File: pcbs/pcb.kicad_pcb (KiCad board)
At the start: 2 copper layers, 148.3 x 111.7 mm, 42 parts

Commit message: Convert to Helios (RP2040-based) MCU and add underglow LEDs
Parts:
- removed the ? at (25.7, 7.11) (x4)
- removed J9: , lib:Jumper
- added ?: LOGO, Library:fractalxcu, F.Cu at (153.4, 156.2)
- added ?: LOGO, Library:fractalx, F.Cu at (153.4, 156.2)
- added ?: LOGO, Library:fractalxcu, B.Cu at (153.4, 156.2)
- added ?: LOGO, Library:fractalx, B.Cu at (153.4, 156.2)
- added J1: , lib:Jumper, F.Cu at (219.8, 129.8)
- added LED1, LED7: , WS2812B, F.Cu at (128.8, 99.8)
- added LED10, LED4: , WS2812B, F.Cu at (149.0, 132.1)
- added LED11, LED5: , WS2812B, F.Cu at (188.8, 102.6)
- added LED12, LED6: , WS2812B, F.Cu at (188.8, 140.6)
- added LED2, LED8: , WS2812B, F.Cu at (128.8, 137.8)
- added LED3, LED9: , WS2812B, F.Cu at (149.4, 94.1)
- MCU1: footprint Elite-C -> Helios
- moved J2 181.5 mm to (221.8, 129.8)
- moved J3 181.5 mm to (223.8, 129.8)
- moved J4 181.5 mm to (225.8, 129.8)
- moved J6 181.5 mm to (221.8, 131.8)
- moved J7 181.5 mm to (223.8, 131.8)
- moved J8 181.5 mm to (225.8, 131.8)
- moved CIRQUE 180.3 mm to (223.8, 133.3)
- moved MCU1 180.3 mm to (207.8, 108.1), turned to 0 degrees
- moved O2 180.3 mm to (218.8, 135.8)
- moved ROT1 180.3 mm to (207.8, 135.6)
- moved S1 180.3 mm to (108.8, 143.8)
- moved S10 180.3 mm to (168.8, 131.8)
- moved S11 180.3 mm to (168.8, 112.8)
- moved S12 180.3 mm to (168.8, 93.8)
- moved S13 180.3 mm to (188.8, 134.6)
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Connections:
- net D0 renamed IO2
- J2 pad 1: O2 -> O5
- J2 pad 2: B2 -> IO20
- J3 pad 1: O5 -> O4
- J3 pad 2: B3 -> GND
- J4 pad 1: O4 -> O3
- J4 pad 2: GND -> IO22
- J5 pad 1: O3 -> T1
- J5 pad 2: B1 -> GND
- J6 pad 1: T1 -> T2
- J6 pad 2: GND -> VCC
- J7 pad 1: T2 -> T3
- J7 pad 2: VCC -> IO3
- J8 pad 1: T3 -> T4
- MCU1 pad 1: D3 -> IO10
- MCU1 pad 10: E6 -> IO6
- MCU1 pad 11: B4 -> IO7
- MCU1 pad 12: B5 -> IO8
- MCU1 pad 13: B6 -> IO9
- MCU1 pad 14: B2 -> IO12
- MCU1 pad 15: B3 -> IO13
- MCU1 pad 16: B1 -> IO14
- MCU1 pad 17: F7 -> IO15
- MCU1 pad 18: F6 -> IO16
- MCU1 pad 19: F5 -> IO21
- MCU1 pad 2: D2 -> TX
- MCU1 pad 20: F4 -> IO23
- MCU1 pad 21: VCC -> IO20
- MCU1 pad 22: ST -> IO22
- MCU1 pad 23: GND -> A0
- MCU1 pad 24: B0 -> A1
- MCU1 pad 25: B7 -> A2
- MCU1 pad 26: D5 -> A3
- MCU1 pad 27: C7 -> VCC
- MCU1 pad 28: F1 -> RST
- MCU1 pad 29: F0 -> GND
- MCU1 pad 3: GND -> RX
- MCU1 pad 5: D1 -> GND
- MCU1 pad 7: D4 -> IO3
- MCU1 pad 8: C6 -> IO4
- MCU1 pad 9: D7 -> IO5
- S1 pad 1: B6 -> IO21
- S10 pad 1: B4 -> IO8
- S11 pad 1: C6 -> IO5
- S12 pad 1: D2 -> IO10
- S13 pad 1: B5 -> IO9
- S14 pad 1: D7 -> IO6
- S15 pad 1: F6 -> RX
- S16 pad 1: F4 -> A3
- S17 pad 1: F5 -> A2
- S18 pad 1: F7 -> A0
- S2 pad 1: F0 -> IO16
- S3 pad 1: F1 -> IO15
- S4 pad 1: C7 -> IO12
- S5 pad 1: D5 -> IO13
- S6 pad 1: B7 -> IO14
- S7 pad 1: E6 -> IO7
- S8 pad 1: D4 -> IO4
- S9 pad 1: F7 -> A1
- TRRS1 pad 3: D3 -> TX
- _1 pad 1: ST -> RST
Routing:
- net VCC: track 68.0 -> 332.6 mm, vias 0 -> 6
- net IO14: track 0.00 -> 186.8 mm, vias 0 -> 1
- net IO13: track 0.00 -> 167.2 mm, vias 0 -> 1
- net F7: track 166.4 -> 0.00 mm, vias 2 -> 0
- net IO15: track 0.00 -> 165.6 mm, vias 0 -> 1
- net F1: track 154.1 -> 0.00 mm, vias 1 -> 0
- net IO16: track 0.00 -> 150.1 mm, vias 0 -> 1
- net IO12: track 0.00 -> 141.8 mm, vias 0 -> 1
- net F0: track 138.7 -> 0.00 mm, vias 1 -> 0
- net B7: track 138.0 -> 0.00 mm, vias 1 -> 0
- net IO21: track 0.00 -> 137.1 mm, vias 0 -> 1
- net B6: track 125.2 -> 0.00 mm, vias 1 -> 0
- net D5: track 122.0 -> 0.00 mm, vias 1 -> 0
- net A0: track 0.00 -> 109.0 mm, vias 0 -> 2
- net C7: track 106.2 -> 0.00 mm, vias 1 -> 0
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
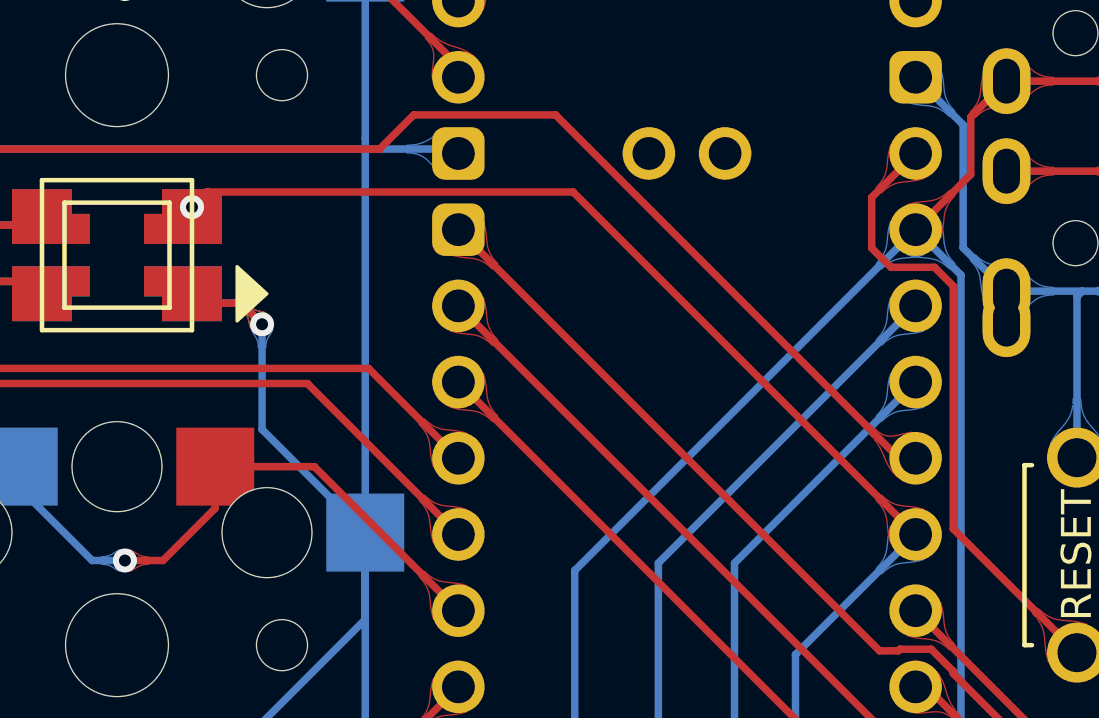
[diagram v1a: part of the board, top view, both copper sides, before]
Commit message: Fix via overlapping with pad
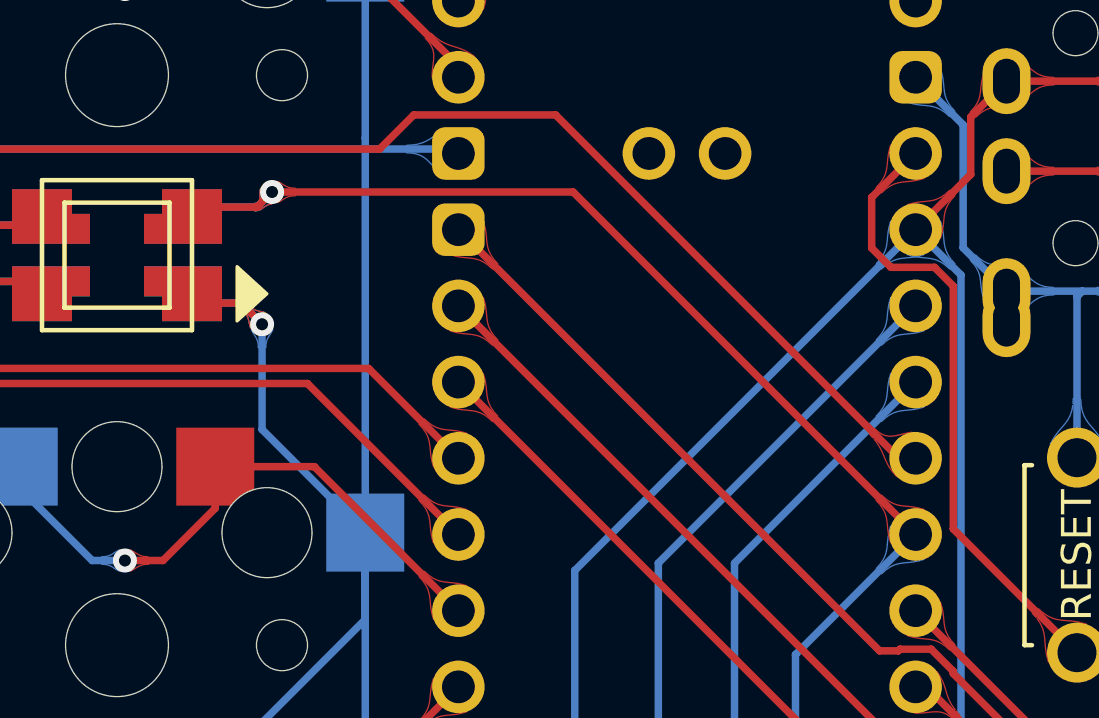
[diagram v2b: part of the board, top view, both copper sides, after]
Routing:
- net A0: track 109.0 -> 111.8 mm
